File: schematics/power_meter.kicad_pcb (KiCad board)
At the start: 2 copper layers, 65 x 56.5 mm, 113 parts, among them J1 EEPROM WE, J2 40HAT, P1 3mm mounting hole, P10 INPUT 5, P11 INPUT 6, P12 INPUT 7, P13 OSHW LOGO, P14 KICAD LOGO, P15 JC128, P16 JC128, P17 JC128, P18 JC128, P19 JC128, P2 3mm mounting hole, P20 JC128, P21 JC128, P22 JC128, P3 3mm mounting hole, P4 3mm mounting hole, P5 INPUT 0, P6 INPUT 1, P7 INPUT 2, P8 INPUT 3, P9 INPUT 4, U1 CAT24C32, U2 MCP3008

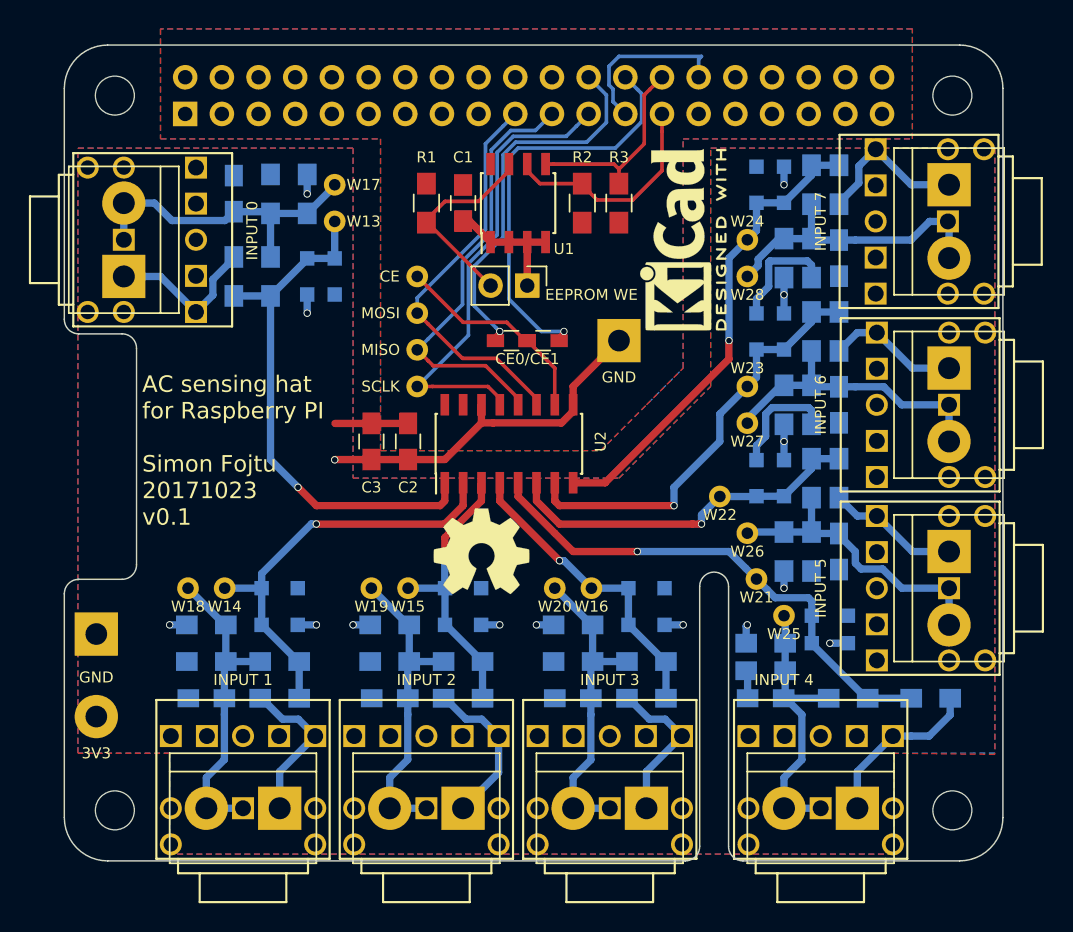
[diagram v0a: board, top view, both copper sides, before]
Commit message: fixup - input connected to virtual ground when no jack connector is inserted
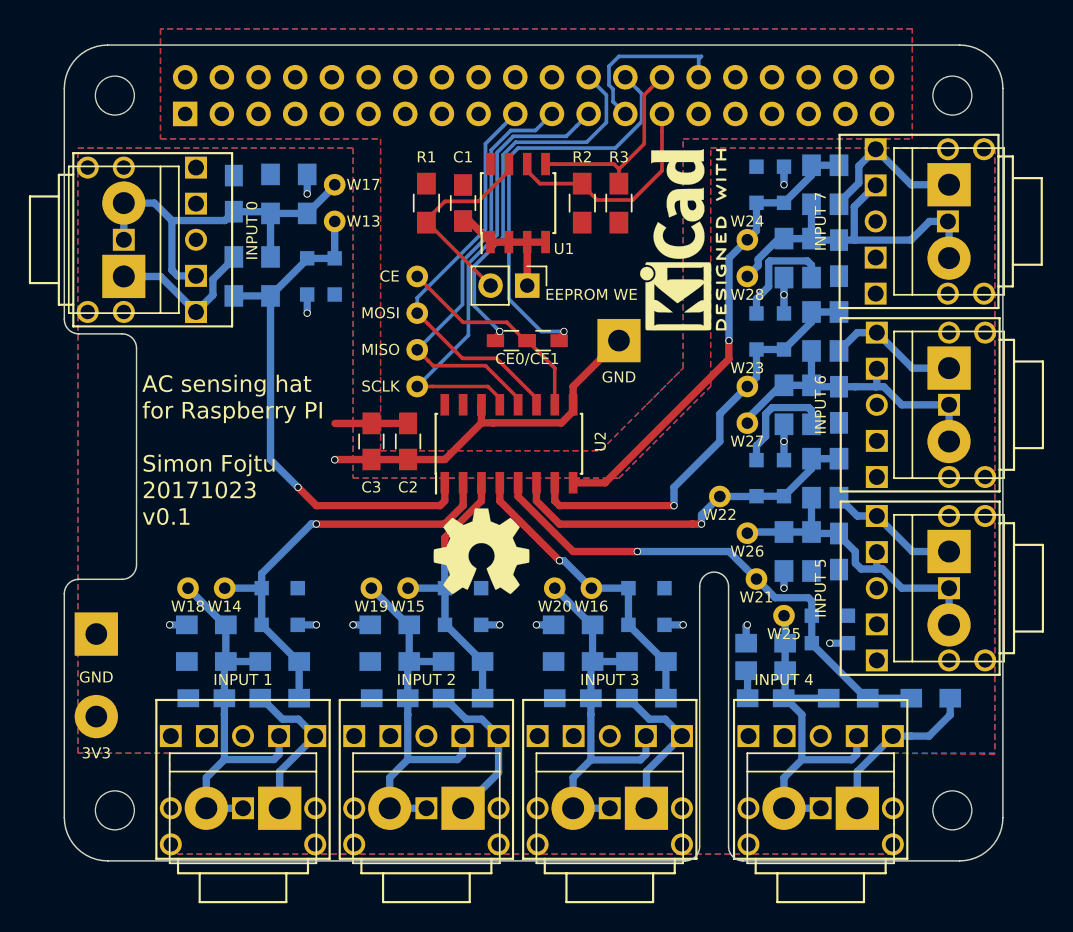
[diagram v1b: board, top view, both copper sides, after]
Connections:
- P15 pad 3: (no net) -> Net-(C4-Pad1)
- P16 pad 3: (no net) -> Net-(C5-Pad1)
- P17 pad 3: (no net) -> Net-(C6-Pad1)
- P18 pad 3: (no net) -> Net-(C7-Pad1)
- P19 pad 3: (no net) -> Net-(C8-Pad1)
- P20 pad 3: (no net) -> Net-(C9-Pad1)
- P21 pad 3: (no net) -> Net-(C10-Pad1)
- P22 pad 3: (no net) -> Net-(C11-Pad1)
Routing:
- net Net-(C4-Pad1): track 21.8 -> 27.1 mm
- net Net-(C7-Pad1): track 21.9 -> 27.1 mm
- net Net-(C8-Pad1): track 20.2 -> 25.4 mm
- net Net-(C6-Pad1): track 21.9 -> 27.1 mm
- net Net-(C5-Pad1): track 21.9 -> 27.1 mm
- net Net-(C11-Pad1): track 20.8 -> 25.2 mm
- net Net-(C10-Pad1): track 20.7 -> 22.0 mm
- net Net-(C9-Pad1): track 21.1 -> 22.3 mm

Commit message: fixup - silkscreen labels position, terminal blocks footprint rotated
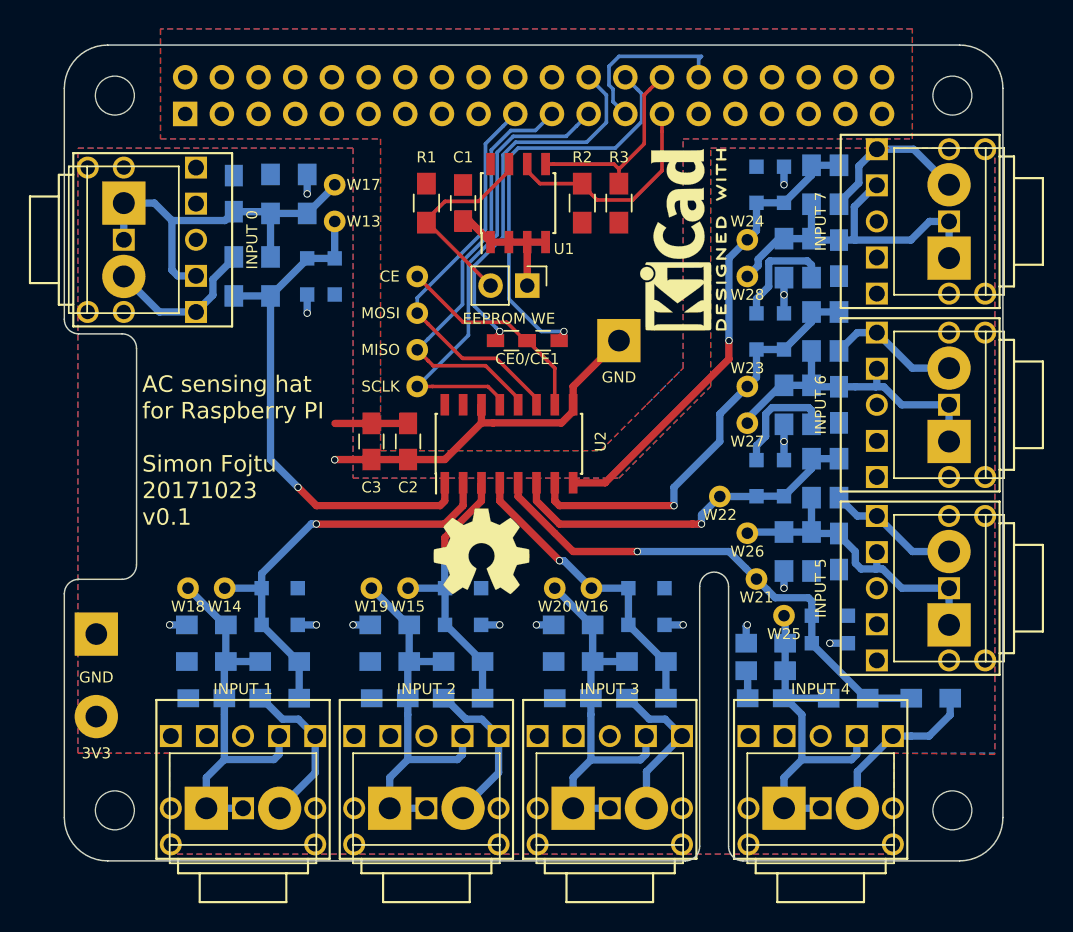
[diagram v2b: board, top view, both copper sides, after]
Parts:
- moved P5 5.08 mm to (71.1, 67.9), turned to 270 degrees
- moved P6 5.08 mm to (76.8, 109.9), turned to 0 degrees
- moved P10 5.08 mm to (128.3, 97.2), turned to 90 degrees
- moved P11 5.08 mm to (128.3, 84.5), turned to 90 degrees
- moved P12 5.08 mm to (128.3, 71.8), turned to 90 degrees
- moved P7 5.08 mm to (89.5, 109.9), turned to 0 degrees
- moved P8 5.08 mm to (102.2, 109.9), turned to 0 degrees
- moved P9 5.08 mm to (116.8, 109.9), turned to 0 degrees
- moved P22 0.08 mm to (123.3, 69.2)
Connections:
- P10 pad 1: Net-(P10-Pad1) -> Net-(C9-Pad1)
- P10 pad 2: Net-(C9-Pad1) -> Net-(P10-Pad2)
- P11 pad 1: Net-(P11-Pad1) -> Net-(C10-Pad1)
- P11 pad 2: Net-(C10-Pad1) -> Net-(P11-Pad2)
- P12 pad 1: Net-(P12-Pad1) -> Net-(C11-Pad1)
- P12 pad 2: Net-(C11-Pad1) -> Net-(P12-Pad2)
- P20 pad 2: Net-(P10-Pad1) -> Net-(P10-Pad2)
- P21 pad 2: Net-(P11-Pad1) -> Net-(P11-Pad2)
- P22 pad 2: Net-(P12-Pad1) -> Net-(P12-Pad2)
- P5 pad 1: Net-(P15-Pad2) -> Net-(C4-Pad1)
- P5 pad 2: Net-(C4-Pad1) -> Net-(P15-Pad2)
- P6 pad 1: Net-(P16-Pad2) -> Net-(C5-Pad1)
- P6 pad 2: Net-(C5-Pad1) -> Net-(P16-Pad2)
- P7 pad 1: Net-(P17-Pad2) -> Net-(C6-Pad1)
- P7 pad 2: Net-(C6-Pad1) -> Net-(P17-Pad2)
- P8 pad 1: Net-(P18-Pad2) -> Net-(C7-Pad1)
- P8 pad 2: Net-(C7-Pad1) -> Net-(P18-Pad2)
- P9 pad 1: Net-(P19-Pad2) -> Net-(C8-Pad1)
- P9 pad 2: Net-(C8-Pad1) -> Net-(P19-Pad2)
- R33 pad 1: Net-(P10-Pad1) -> Net-(P10-Pad2)
- R34 pad 1: Net-(P11-Pad1) -> Net-(P11-Pad2)
- R35 pad 1: Net-(P12-Pad1) -> Net-(P12-Pad2)
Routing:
- net Net-(P12-Pad2): track 0.00 -> 11.0 mm
- net Net-(P12-Pad1): track 11.0 -> 0.00 mm
- net Net-(P10-Pad2): track 0.00 -> 9.17 mm
- net Net-(P10-Pad1): track 9.17 -> 0.00 mm
- net Net-(P11-Pad2): track 0.00 -> 9.17 mm
- net Net-(P11-Pad1): track 9.17 -> 0.00 mm
